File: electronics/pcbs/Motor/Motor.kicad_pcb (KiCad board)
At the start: 2 copper layers, 123.8 x 53.3 mm, 13 parts, among them J1 Left Encoder, J2 Right Encoder, J3 I2C Bus, P1 Power, P2 Analog, P3 Digital, P4 Digital, P5 CONN_01X01, P6 CONN_01X01, P7 CONN_01X01, P8 CONN_01X01, U1 Left Nano, U2 Right Nano

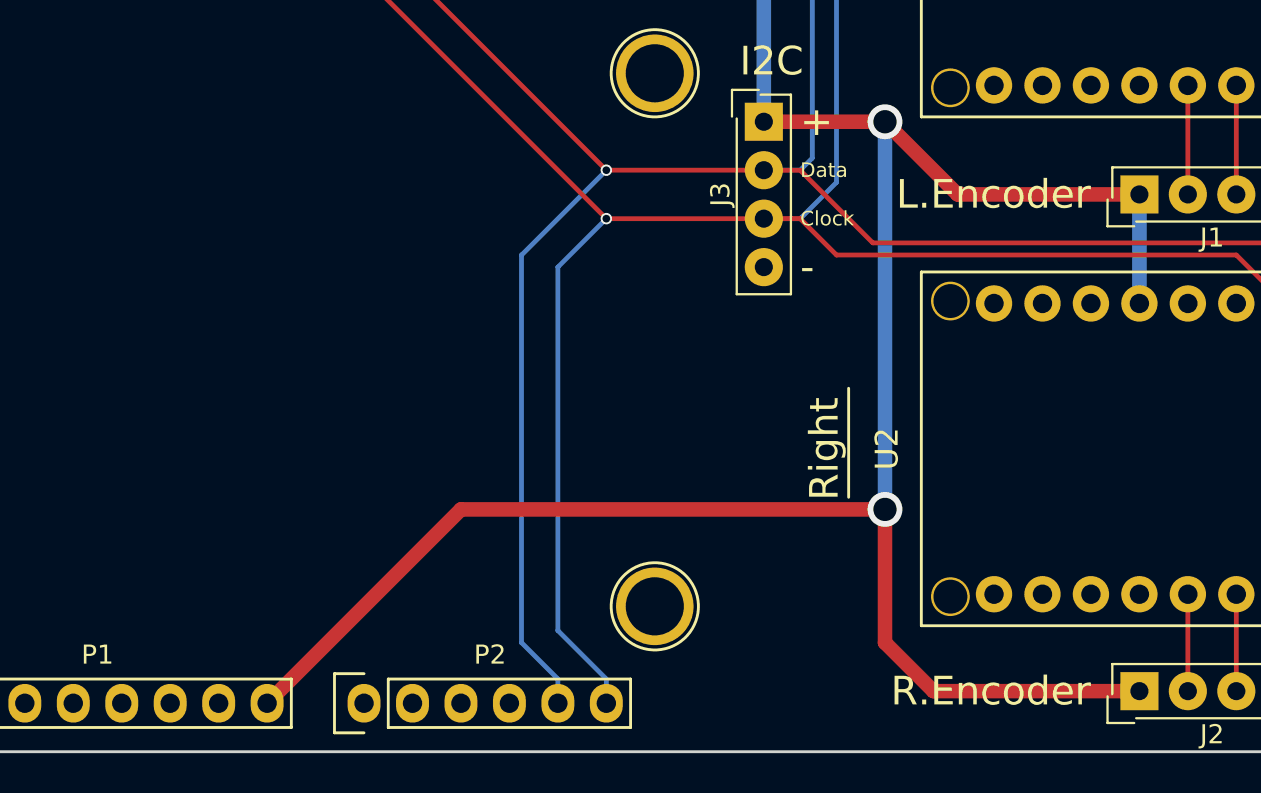
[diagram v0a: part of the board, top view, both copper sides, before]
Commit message: Motor PCB: Uno is now powered by BATT+; added screw terminal for battery input.
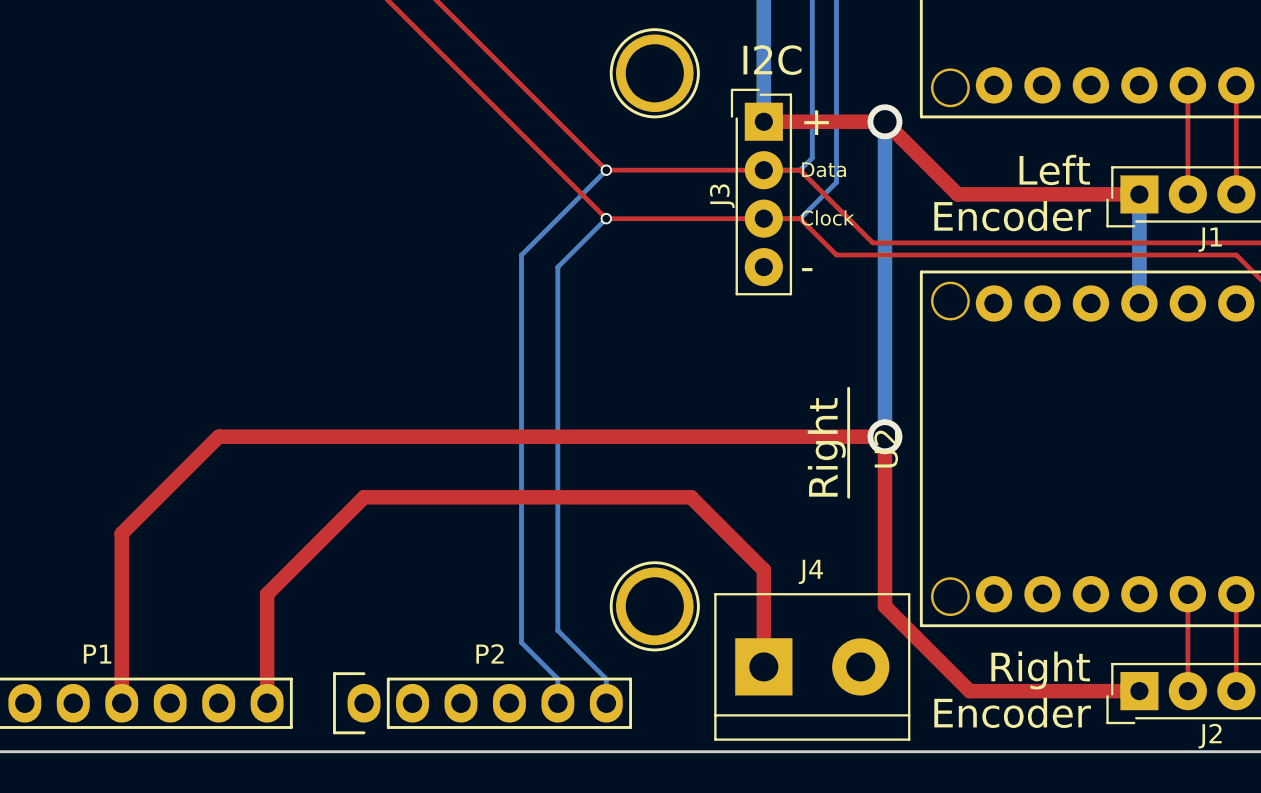
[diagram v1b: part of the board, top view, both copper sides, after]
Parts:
- added J4: Battery, Connectors_Terminal_Blocks:TerminalBlock_bornier-2_P5.08mm, F.Cu at (182.8, 121.9)
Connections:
- net /IOREF renamed Net-(P1-Pad2)
- P1 pad 5: Net-(P1-Pad5) -> +5V
- P1 pad 8: +5V -> +BATT
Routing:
- net +BATT: track 0.00 -> 40.5 mm
- net +5V: track 138.4 -> 151.7 mm
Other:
- board text added: "Left Encoder"
- board text added: "Right Encoder"
- board text removed: "L.Encoder"
- board text removed: "R.Encoder"

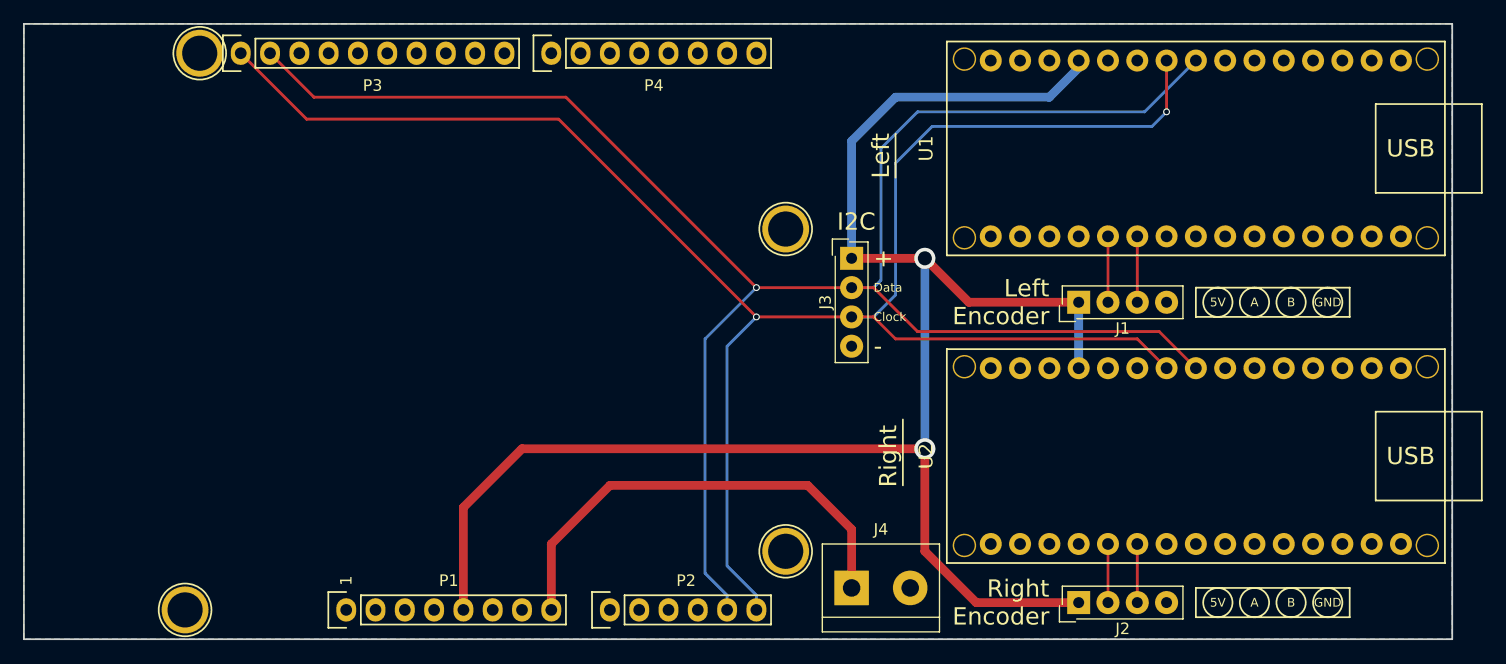
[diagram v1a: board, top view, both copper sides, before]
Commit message: Motor PCB: Added silkscreen label for battery and its polarity. Hid PX and UX labels for Arduino headers.
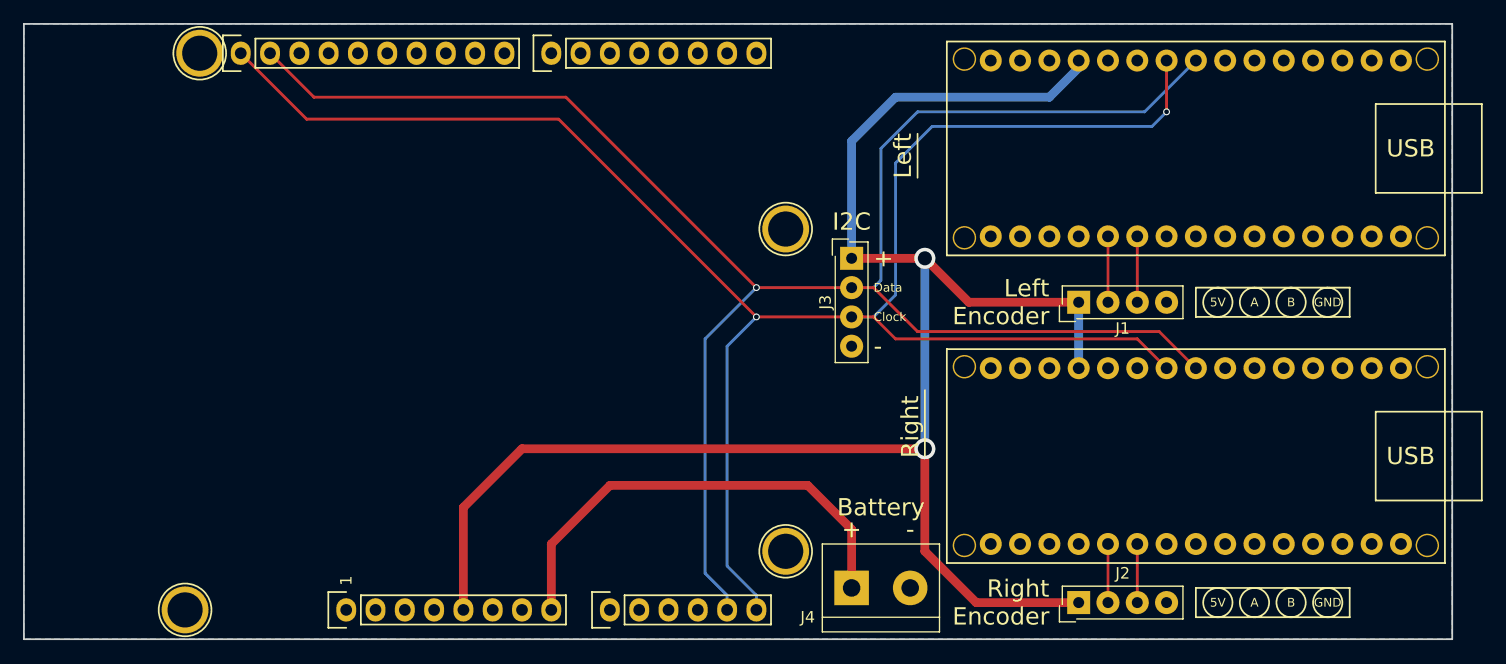
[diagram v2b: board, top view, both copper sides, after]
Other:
- board text added: "Battery"
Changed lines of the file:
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@@
     (links 40)
     (no_connects 0)
-    (area 110.922999 72.949999 234.898001 126.440001)
+    (area 104.572999 71.542 237.663001 128.075)
     (thickness 1.6)
-    (drawings 71)
+    (drawings 74)
     (tracks 68)
     (zones 0)
@@
       (outputformat 1)
       (mirror false)
-      (drillshape 1)
+      (drillshape 0)
       (scaleselection 1)
-      (outputdirectory ""))
+      (outputdirectory ./Output))
   )
   (net 0 "")
@@
   (module Arduino_Nano:Arduino_Nano (layer F.Cu)
     (at 234.188 76.2)
-    (fp_text reference U1 (at -44.98 7.62 90) (layer F.SilkS)
+    (fp_text reference U1 (at -44.98 7.62 90) (layer F.SilkS) hide
       (effects (font (size 1.2 1.2) (thickness 0.15)))
     )
@@
     (descr "Through hole socket strip")
     (tags "socket strip")
-    (fp_text reference P1 (at 8.89 -2.54) (layer F.SilkS)
+    (fp_text reference P1 (at 8.89 -2.54) (layer F.SilkS) hide
       (effects (font (size 1 1) (thickness 0.15)))
     )
@@
     (descr "Through hole socket strip")
     (tags "socket strip")
-    (fp_text reference P2 (at 6.604 -2.54) (layer F.SilkS)
+    (fp_text reference P2 (at 6.604 -2.54) (layer F.SilkS) hide
       (effects (font (size 1 1) (thickness 0.15)))
     )
@@
     (descr "Through hole socket strip")
     (tags "socket strip")
-    (fp_text reference P3 (at 11.43 2.794) (layer F.SilkS)
+    (fp_text reference P3 (at 11.43 2.794) (layer F.SilkS) hide
       (effects (font (size 1 1) (thickness 0.15)))
     )
@@
     (descr "Through hole socket strip")
     (tags "socket strip")
-    (fp_text reference P4 (at 8.89 2.794) (layer F.SilkS)
+    (fp_text reference P4 (at 8.89 2.794) (layer F.SilkS) hide
       (effects (font (size 1 1) (thickness 0.15)))
     )
@@
     (descr "Low profile, screw machine socket strip, through hole, 100mil / 2.54mm pitch")
     (tags "samtec socket strip tht single")
-    (fp_text reference J2 (at -2.27 3.81 180) (layer F.SilkS)
+    (fp_text reference J2 (at 2.54 3.81 180) (layer F.SilkS)
       (effects (font (size 1 1) (thickness 0.15)))
     )
@@
   (module Arduino_Nano:Arduino_Nano (layer F.Cu)
     (at 234.188 102.87)
-    (fp_text reference U2 (at -44.98 7.62 90) (layer F.SilkS)
+    (fp_text reference U2 (at -44.98 7.62 90) (layer F.SilkS) hide
       (effects (font (size 1.2 1.2) (thickness 0.15)))
     )
@@
     (descr "simple 2-pin terminal block, pitch 5.08mm, revamped version of bornier2")
     (tags "terminal block bornier2")
-    (fp_text reference J4 (at 2.54 -5.08) (layer F.SilkS)
+    (fp_text reference J4 (at -3.81 2.54) (layer F.SilkS)
       (effects (font (size 1 1) (thickness 0.15)))
     )
@@
     )
   )
+  (gr_text - (at 187.833 116.84) (layer F.SilkS)
+    (effects (font (size 1.5 1.5) (thickness 0.3)))
+  )
+  (gr_text + (at 182.753 116.84) (layer F.SilkS)
+    (effects (font (size 1.5 1.5) (thickness 0.3)))
+  )
+  (gr_text Battery (at 185.293 114.935) (layer F.SilkS)
+    (effects (font (size 1.5 1.5) (thickness 0.3)))
+  )
   (gr_text USB (at 229.108 110.49) (layer F.SilkS)
     (effects (font (size 1.5 1.5) (thickness 0.3)) (justify left))
@@
     (effects (font (size 1.5 1.5) (thickness 0.3)) (justify right))
   )
-  (gr_text I2C (at 181.483 90.17) (layer F.SilkS)
-    (effects (font (size 1.5 1.5) (thickness 0.3)) (justify left))
-  )
-  (gr_line (start 187.198 107.315) (end 187.198 113.03) (angle 90) (layer F.SilkS) (width 0.15))
-  (gr_line (start 186.563 82.55) (end 186.563 86.36) (angle 90) (layer F.SilkS) (width 0.15))
-  (gr_text Right (at 185.928 110.49 90) (layer F.SilkS)
+  (gr_text I2C (at 182.753 90.17) (layer F.SilkS)
     (effects (font (size 1.5 1.5) (thickness 0.3)))
   )
-  (gr_text Left (at 185.293 84.455 90) (layer F.SilkS)
+  (gr_line (start 189.103 104.775) (end 189.103 110.49) (angle 90) (layer F.SilkS) (width 0.15))
+  (gr_line (start 188.468 82.55) (end 188.468 86.36) (angle 90) (layer F.SilkS) (width 0.15))
+  (gr_text Right (at 187.833 107.95 90) (layer F.SilkS)
     (effects (font (size 1.5 1.5) (thickness 0.3)))
   )
+  (gr_text Left (at 187.198 84.455 90) (layer F.SilkS)
+    (effects (font (size 1.5 1.5) (thickness 0.3)))
+  )
